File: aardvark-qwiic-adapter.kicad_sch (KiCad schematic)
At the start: 2 parts, among them J1 Conn_02x05_Odd_Even, J2 Conn_01x03

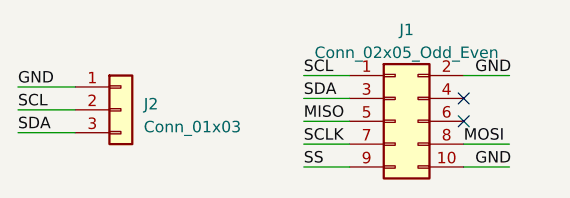
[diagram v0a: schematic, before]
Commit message: Remove I2C, relabel for GPIO
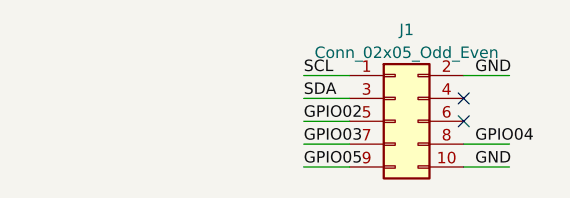
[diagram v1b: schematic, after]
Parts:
- removed J2: Conn_01x03, Connector_PinHeader_2.54mm:PinHeader_1x03_P2.54mm_Vertical, symbol Connector_Generic:Conn_01x03
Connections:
- net MISO renamed GPIO02
- net MOSI renamed GPIO04
- net SCLK renamed GPIO03
- net SS renamed GPIO05
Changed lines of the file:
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@@
-    (stroke (width 0) (type default))
-  )
-  (wire (pts (xy 99.06 92.71) (xy 105.41 92.71))
     (stroke (width 0) (type default))
   )
@@
     (stroke (width 0) (type default))
   )
-  (wire (pts (xy 99.06 97.79) (xy 105.41 97.79))
+  (wire (pts (xy 130.81 96.52) (xy 135.89 96.52))
     (stroke (width 0) (type default))
   )
-  (wire (pts (xy 99.06 95.25) (xy 105.41 95.25))
-    (stroke (width 0) (type default))
-  )
-  (wire (pts (xy 130.81 96.52) (xy 135.89 96.52))
-    (stroke (width 0) (type default))
+  (label "GPIO05" (at 130.81 101.6 0) (fields_autoplaced)
+    (effects (font (size 1.27 1.27)) (justify left bottom))
   )
   (label "SCL" (at 130.81 91.44 0) (fields_autoplaced)
     (effects (font (size 1.27 1.27)) (justify left bottom))
   )
-  (label "GND" (at 99.06 92.71 0) (fields_autoplaced)
+  (label "GPIO04" (at 149.86 99.06 0) (fields_autoplaced)
     (effects (font (size 1.27 1.27)) (justify left bottom))
   )
@@
     (effects (font (size 1.27 1.27)) (justify left bottom))
   )
-  (label "SCLK" (at 130.81 99.06 0) (fields_autoplaced)
-    (effects (font (size 1.27 1.27)) (justify left bottom))
-  )
-  (label "SS" (at 130.81 101.6 0) (fields_autoplaced)
+  (label "GPIO02" (at 130.81 96.52 0) (fields_autoplaced)
     (effects (font (size 1.27 1.27)) (justify left bottom))
   )
@@
     (effects (font (size 1.27 1.27)) (justify left bottom))
   )
-  (label "SDA" (at 99.06 97.79 0) (fields_autoplaced)
-    (effects (font (size 1.27 1.27)) (justify left bottom))
-  )
-  (label "MOSI" (at 148.59 99.06 0) (fields_autoplaced)
-    (effects (font (size 1.27 1.27)) (justify left bottom))
-  )
-  (label "MISO" (at 130.81 96.52 0) (fields_autoplaced)
+  (label "GPIO03" (at 130.81 99.06 0) (fields_autoplaced)
     (effects (font (size 1.27 1.27)) (justify left bottom))
   )
   (label "GND" (at 149.86 91.44 0) (fields_autoplaced)
     (effects (font (size 1.27 1.27)) (justify left bottom))
-  )
-  (label "SCL" (at 99.06 95.25 0) (fields_autoplaced)
-    (effects (font (size 1.27 1.27)) (justify left bottom))
-  )
-  (symbol (lib_id "Connector_Generic:Conn_01x03") (at 110.49 95.25 0) (unit 1)
-    (in_bom yes) (on_board yes) (dnp no) (fields_autoplaced)
-    (property "Reference" "J2" (at 113.03 94.615 0)
-      (effects (font (size 1.27 1.27)) (justify left))
-    )
-    (property "Value" "Conn_01x03" (at 113.03 97.155 0)
-      (effects (font (size 1.27 1.27)) (justify left))
-    )
-    (property "Footprint" "Connector_PinHeader_2.54mm:PinHeader_1x03_P2.54mm_Vertical" (at 110.49 95.25 0)
-      (effects (font (size 1.27 1.27)) hide)
-    )
-    (property "Datasheet" "~" (at 110.49 95.25 0)
-      (effects (font (size 1.27 1.27)) hide)
-    )
-    (pin "1")
-    (pin "2")
-    (pin "3")
-    (instances
-      (project "aardvark-i2c-breakout"
-        (path "/dd35b9f1-2797-46a7-a3ff-4e2c1be5fc91"
-          (reference "J2") (unit 1)
-        )
-      )
-    )
   )
   (symbol (lib_id "Connector_Generic:Conn_02x05_Odd_Even") (at 140.97 96.52 0) (unit 1)
@@
     (pin "9")
     (instances
-      (project "aardvark-i2c-breakout"
+      (project "aardvark-qwiic-adapter"
         (path "/dd35b9f1-2797-46a7-a3ff-4e2c1be5fc91"
           (reference "J1") (unit 1)
